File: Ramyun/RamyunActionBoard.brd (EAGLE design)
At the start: 135.2 x 135.2 mm, 78 parts, among them Q1 BC817-16LT1SMD, Q2 BC817-16LT1SMD, Q3 NVF6P02, U1 MAX31856_ADAFRUIT, U10 PVN012PBF, U11 PVN012PBF, U12 PVN012PBF, U13 PVN012PBF, U2 MAX31856_ADAFRUIT, U3 NL17SZ17, U4 GPS_ADAFRUIT, U5 BUZZER, U6 PVN012PBF, U7 PVN012PBF, U8 PVN012PBF, U9 PVN012PBF, X1 5267-03, X10 5267-02, X11 5267-02, X12 5267-02, X13 5267-02, X14 5267-02, X15 5267-02, X16 5267-02, X2 5267-03, X3 5267-03, X4 USB+SHIELD, X5 5267-02, X6 5267-02, X7 5267-02, X8 5267-02, X9 5267-02

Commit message: tired 2
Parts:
- added TP1, TP2, TP3, TP4, TP5, TP6: (no value), berry:TP-5010
- moved D1 15.3 mm to (52.1, 7.62)
- moved R5 5.68 mm to (15.2, -27.9), turned to 90 degrees
- moved R4 1.27 mm to (-10.2, -16.5)
- moved R7 1.27 mm to (-2.54, -16.5)
- moved R8 1.27 mm to (0.00, -16.5)
- moved C1 1.27 mm to (24.1, -25.4)
- moved JP2 1.27 mm to (-22.9, -17.8)
- moved JP4 1.27 mm to (22.9, -17.8)
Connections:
- net +5V: now also TP1.TP
- net GND: now also TP4.TP
- net GND_EXT1: now also TP5.TP
- net GND_EXT2: now also TP6.TP
- net V_EXT1: now also TP2.TP
- net V_EXT2: now also TP3.TP
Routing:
- net +5V: track 0.00 -> 205.8 mm, vias 0 -> 2
- net GND_EXT2: track 0.00 -> 151.3 mm
- net GND_EXT1: track 0.00 -> 143.8 mm
- net HP_OUT: track 0.00 -> 119.1 mm, vias 0 -> 1
- net +3V3: track 0.00 -> 97.5 mm, vias 0 -> 1
- net V_EXT2: track 0.00 -> 94.1 mm
- net V_EXT1: track 0.00 -> 93.4 mm
- net SERVO_1: track 0.00 -> 66.0 mm, vias 0 -> 1
- net LED1: track 0.00 -> 59.6 mm, vias 0 -> 1
- net OUT_A1: track 0.00 -> 55.1 mm, vias 0 -> 1
- net TEMP1_CS: track 0.00 -> 53.8 mm, vias 0 -> 1
- net MISO: track 0.00 -> 52.4 mm
- net TEMP2_CS: track 0.00 -> 50.7 mm, vias 0 -> 2
- net OUT_A2: track 0.00 -> 49.6 mm, vias 0 -> 1
- net MOSI: track 0.00 -> 46.0 mm, vias 0 -> 2
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- added copper zone on layer 16, net GND

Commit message: gerber done
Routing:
- net BUZZER: track 34.3 -> 29.4 mm
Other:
- board text added: "5V"
- board text added: "D+"
- board text added: "D-"
- board text added: "GEXT1"
- board text added: "GEXT2"
- board text added: "GND"
- board text added: "HP"
- board text added: "LED"
- board text added: "OUTA1"
- board text added: "OUTA2"
- board text added: "OUTA3"
- board text added: "OUTA4"
- board text added: "OUTB1"
- board text added: "OUTB2"
- board text added: "OUTB3"
- board text added: "OUTB4"
- board text added: "SERVO1"
- board text added: "SERVO2"
- board text added: "SERVO3"
- board text added: "VBUS"
- board text added: "VEXT1"
- board text added: "VEXT2"
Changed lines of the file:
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@@
 <text x="-7.62" y="50.8" size="2.1844" layer="1" font="vector" ratio="10">Project R</text>
 <text x="-7.62" y="50.8" size="2.1844" layer="29" font="vector" ratio="10">Project R</text>
+<text x="44.45" y="-5.08" size="1.27" layer="21" font="vector">VBUS</text>
+<text x="44.45" y="-1.905" size="1.27" layer="21" font="vector">D-</text>
+<text x="44.45" y="0.635" size="1.27" layer="21" font="vector">D+</text>
+<text x="44.45" y="3.175" size="1.27" layer="21" font="vector">GND</text>
+<text x="-39.37" y="-50.165" size="1.27" layer="21" font="vector">VEXT1</text>
+<text x="-39.37" y="-52.705" size="1.27" layer="21" font="vector">GEXT1</text>
+<text x="-64.77" y="-5.08" size="1.27" layer="21" font="vector" rot="SR270">OUTB1</text>
+<text x="-62.23" y="-15.24" size="1.27" layer="21" font="vector" rot="SR270">OUTB2</text>
+<text x="-58.42" y="-25.4" size="1.27" layer="21" font="vector" rot="SR270">OUTB3</text>
+<text x="-50.8" y="-35.56" size="1.27" layer="21" font="vector" rot="SR270">OUTB4</text>
+<text x="-50.8" y="43.18" size="1.27" layer="21" font="vector" rot="SR270">OUTA1</text>
+<text x="-58.42" y="33.02" size="1.27" layer="21" font="vector" rot="SR270">OUTA2</text>
+<text x="-62.23" y="21.59" size="1.27" layer="21" font="vector" rot="SR270">OUTA3</text>
+<text x="-64.77" y="12.7" size="1.27" layer="21" font="vector" rot="SR270">OUTA4</text>
+<text x="-39.37" y="48.895" size="1.27" layer="21" font="vector">GEXT2</text>
+<text x="-39.37" y="51.435" size="1.27" layer="21" font="vector">VEXT2</text>
+<text x="48.895" y="40.005" size="1.27" layer="21" font="vector" rot="R90">HP</text>
+<text x="62.23" y="15.24" size="1.27" layer="21" font="vector" rot="R90">5V</text>
+<text x="62.23" y="17.78" size="1.27" layer="21" font="vector" rot="R90">GND</text>
+<text x="62.23" y="-19.05" size="1.27" layer="21" font="vector" rot="R90">SERVO1</text>
+<text x="58.42" y="-31.75" size="1.27" layer="21" font="vector" rot="R90">SERVO2</text>
+<text x="49.53" y="-43.18" size="1.27" layer="21" font="vector" rot="R90">SERVO3</text>
+<text x="55.88" y="31.75" size="1.27" layer="21" font="vector" rot="R90">LED</text>
 </plain>
 <attributes>
@@
 <contactref element="MS1" pad="23"/>
 <wire x1="15.24" y1="-29.09" x2="15.24" y2="-29.21" width="0.3048" layer="1"/>
-<wire x1="15.24" y1="-29.21" x2="13.97" y2="-30.48" width="0.3048" layer="1"/>
-<wire x1="13.97" y1="-30.48" x2="12.7" y2="-30.48" width="0.3048" layer="1"/>
-<wire x1="12.7" y1="-30.48" x2="11.43" y2="-29.21" width="0.3048" layer="1"/>
 <wire x1="11.5" y1="-25.5" x2="15" y2="-29" width="0.254" layer="1"/>
 <wire x1="11.5" y1="-21.5" x2="11.5" y2="-25.5" width="0.254" layer="1"/>
@@
 <wire x1="58.42" y1="16.53" x2="53.93" y2="16.53" width="1.016" layer="1"/>
 <wire x1="53.93" y1="16.53" x2="52.68" y2="17.78" width="1.016" layer="1"/>
-<wire x1="52.5" y1="18" x2="46.5" y2="18" width="0.254" layer="1"/>
-<wire x1="46.5" y1="18" x2="46.38" y2="17.78" width="0.254" layer="1"/>
-<wire x1="52.5" y1="18" x2="52.68" y2="17.78" width="0.254" layer="1"/>
+<wire x1="46.38" y1="17.78" x2="46.5" y2="18" width="0.254" layer="1"/>
+<wire x1="52.68" y1="17.78" x2="52.5" y2="18" width="0.254" layer="1"/>
+<wire x1="52.5" y1="18" x2="46.6" y2="18" width="1.016" layer="1"/>
+<wire x1="46.6" y1="18" x2="46.38" y2="17.78" width="1.016" layer="1"/>
 </signal>
 <signal name="HP_SSR">

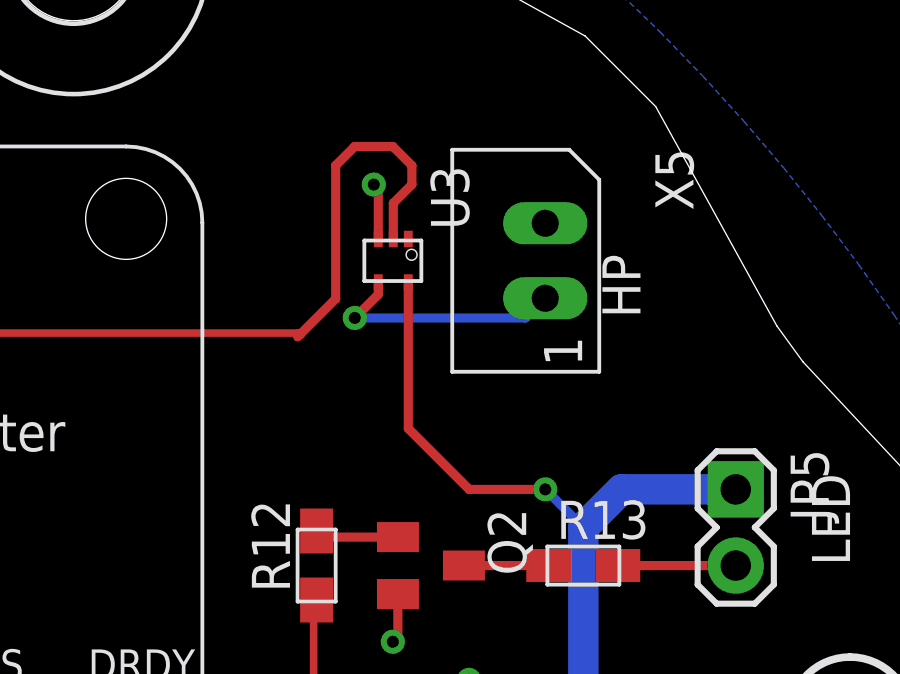
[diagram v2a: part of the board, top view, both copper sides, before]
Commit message: nl17sz17
package added
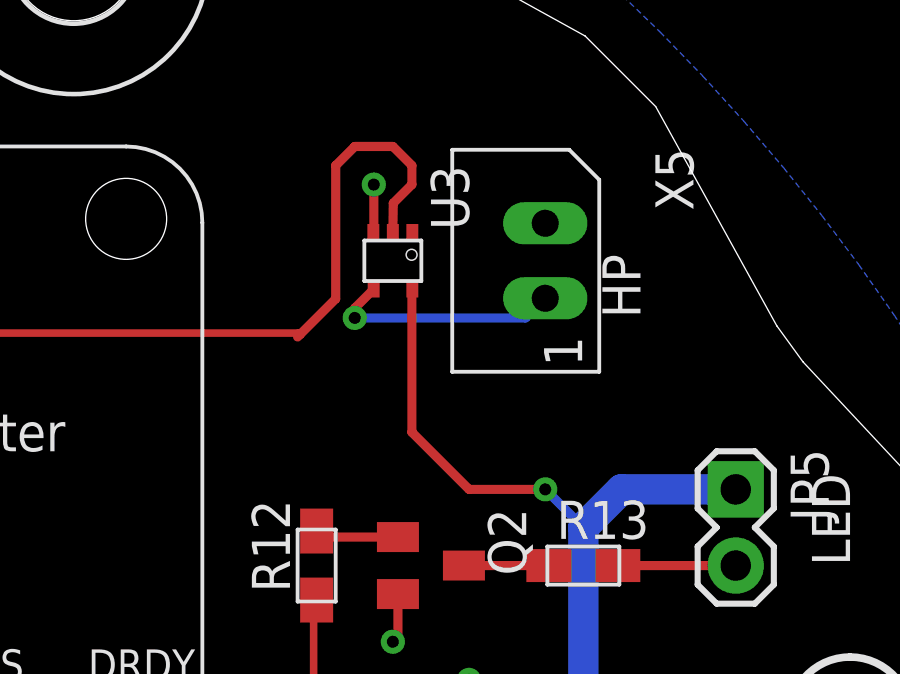
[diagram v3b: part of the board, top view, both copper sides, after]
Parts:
- U3: value NL17SZ17 -> NL17SZ17DFT; device GFE:SOT-553 -> GFE:SOT-353
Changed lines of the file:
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@@
 <element name="X15" library="GFE" package="5267-02" value="5267-02" x="-46.99" y="39.37" rot="R90"/>
 <element name="Q3" library="GFE" package="SOT223" value="NVF6P02" x="49.53" y="17.78" rot="R270"/>
-<element name="U3" library="GFE" package="SOT-553" value="NL17SZ17" x="40.64" y="41.91" rot="R180"/>
+<element name="U3" library="GFE" package="SOT-353" value="NL17SZ17DFT" x="40.64" y="41.91" rot="R180"/>
 <element name="X5" library="GFE" package="5267-02" value="5267-02" x="45.72" y="41.91" rot="R270"/>
 <element name="Q2" library="GFE" package="SOT23-BEC" value="BC817-16LT1SMD" x="41.91" y="31.75" rot="R270"/>
@@
 <wire x1="40.81" y1="30.8" x2="40.81" y2="29.38" width="0.3048" layer="1"/>
 <wire x1="40.81" y1="29.38" x2="40.64" y2="29.21" width="0.3048" layer="1"/>
-<wire x1="40.155" y1="42.635" x2="40.155" y2="44.3" width="0.3048" layer="1"/>
-<wire x1="40.155" y1="44.3" x2="40.005" y2="44.45" width="0.3048" layer="1"/>
 <via x="17.78" y="-30.48" extent="1-16" drill="0.4"/>
 <via x="20.955" y="-25.4" extent="1-16" drill="0.4"/>
@@
 <wire x1="17.95" y1="-28.89" x2="17.95" y2="-30.31" width="0.3048" layer="1"/>
 <wire x1="17.95" y1="-30.31" x2="17.78" y2="-30.48" width="0.3048" layer="1"/>
+<wire x1="39.99" y1="42.86" x2="40.005" y2="42.86" width="0.3048" layer="1"/>
+<wire x1="40.005" y1="42.86" x2="40.005" y2="44.45" width="0.3048" layer="1"/>
 </signal>
 <signal name="+3V3">
@@
 <via x="43.18" y="27.94" extent="1-16" drill="0.4"/>
 <wire x1="43.18" y1="27.94" x2="46.99" y2="27.94" width="0.3048" layer="16"/>
-<wire x1="41.155" y1="41.185" x2="41.155" y2="36.315" width="0.3048" layer="1"/>
-<wire x1="43.18" y1="34.29" x2="45.72" y2="34.29" width="0.3048" layer="1"/>
+<wire x1="45.72" y1="34.29" x2="43.18" y2="34.29" width="0.3048" layer="1"/>
 <via x="45.72" y="34.29" extent="1-16" drill="0.4"/>
 <wire x1="45.72" y1="34.29" x2="46.99" y2="33.02" width="0.3048" layer="16"/>
-<wire x1="41.155" y1="36.315" x2="43.18" y2="34.29" width="0.3048" layer="1"/>
 <wire x1="25.28" y1="-27.94" x2="26.63" y2="-27.94" width="1.016" layer="1"/>
 <wire x1="25.28" y1="-25.4" x2="26.63" y2="-25.4" width="1.016" layer="1"/>
+<wire x1="43.18" y1="34.29" x2="41.275" y2="36.195" width="0.3048" layer="1"/>
+<wire x1="41.275" y1="36.195" x2="41.275" y2="40.945" width="0.3048" layer="1"/>
+<wire x1="41.275" y1="40.945" x2="41.29" y2="40.96" width="0.3048" layer="1"/>
 </signal>
 <signal name="N$19">
@@
 <contactref element="MS1" pad="20"/>
 <contactref element="U3" pad="2"/>
-<wire x1="40.655" y1="42.635" x2="40.655" y2="43.83" width="0.3048" layer="1"/>
+<wire x1="40.64" y1="42.86" x2="40.655" y2="43.83" width="0.3048" layer="1"/>
 <wire x1="40.655" y1="43.83" x2="41.275" y2="44.45" width="0.3048" layer="1"/>
 <wire x1="41.275" y1="44.45" x2="41.275" y2="45.085" width="0.3048" layer="1"/>
@@
 <contactref element="U3" pad="4"/>
 <contactref element="X5" pad="1"/>
-<wire x1="40.155" y1="41.185" x2="40.155" y2="40.79" width="0.3048" layer="1"/>
-<wire x1="40.155" y1="40.79" x2="39.37" y2="40.005" width="0.3048" layer="1"/>
+<wire x1="39.52" y1="40.155" x2="39.37" y2="40.005" width="0.3048" layer="1"/>
 <via x="39.37" y="40.005" extent="1-16" drill="0.4"/>
 <wire x1="39.37" y1="40.005" x2="45.065" y2="40.005" width="0.3048" layer="16"/>
 <wire x1="45.065" y1="40.005" x2="45.72" y2="40.66" width="0.3048" layer="16"/>
+<wire x1="39.37" y1="40.005" x2="39.37" y2="40.33" width="0.3048" layer="1"/>
+<wire x1="39.37" y1="40.33" x2="40" y2="40.96" width="0.3048" layer="1"/>
 </signal>
 <signal name="N$13">

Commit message: value changed
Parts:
- R10, R11, R9: value 4.7k -> 250
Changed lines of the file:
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@@
 <element name="R7" library="GFE" package="R0603(1608)_HANDSOLDER" value="4.7k" x="-2.54" y="-16.51" rot="R270"/>
 <element name="R8" library="GFE" package="R0603(1608)_HANDSOLDER" value="4.7k" x="0" y="-16.51" rot="R270"/>
-<element name="R9" library="GFE" package="R0603(1608)_HANDSOLDER" value="4.7k" x="-11.43" y="16.51" rot="R90"/>
-<element name="R10" library="GFE" package="R0603(1608)_HANDSOLDER" value="4.7k" x="-8.89" y="16.51" rot="R90"/>
-<element name="R11" library="GFE" package="R0603(1608)_HANDSOLDER" value="4.7k" x="-6.35" y="16.51" rot="R90"/>
+<element name="R9" library="GFE" package="R0603(1608)_HANDSOLDER" value="250" x="-11.43" y="16.51" rot="R90"/>
+<element name="R10" library="GFE" package="R0603(1608)_HANDSOLDER" value="250" x="-8.89" y="16.51" rot="R90"/>
+<element name="R11" library="GFE" package="R0603(1608)_HANDSOLDER" value="250" x="-6.35" y="16.51" rot="R90"/>
 <element name="JP3" library="GFE" package="JP2SMD0603" value="JP2" x="22.86" y="-15.24"/>
 <element name="JP4" library="GFE" package="JP2SMD0603" value="JP2" x="22.86" y="-17.78"/>
